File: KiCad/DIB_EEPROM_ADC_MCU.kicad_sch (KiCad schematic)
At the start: 63 parts, among them IC1 ADS131A04IPBSR, IC2 ISO6762FDWR, IC3 ISO6762FDWR, IC4 STM32H503CBT6, IC5 M24C32-DFDW6TP, X1 Edge connector, X2 N.C., Y1 ECS-163.84-10-33-JGN-TR, Y2 ABM8-25.000MHZ-D2X-T

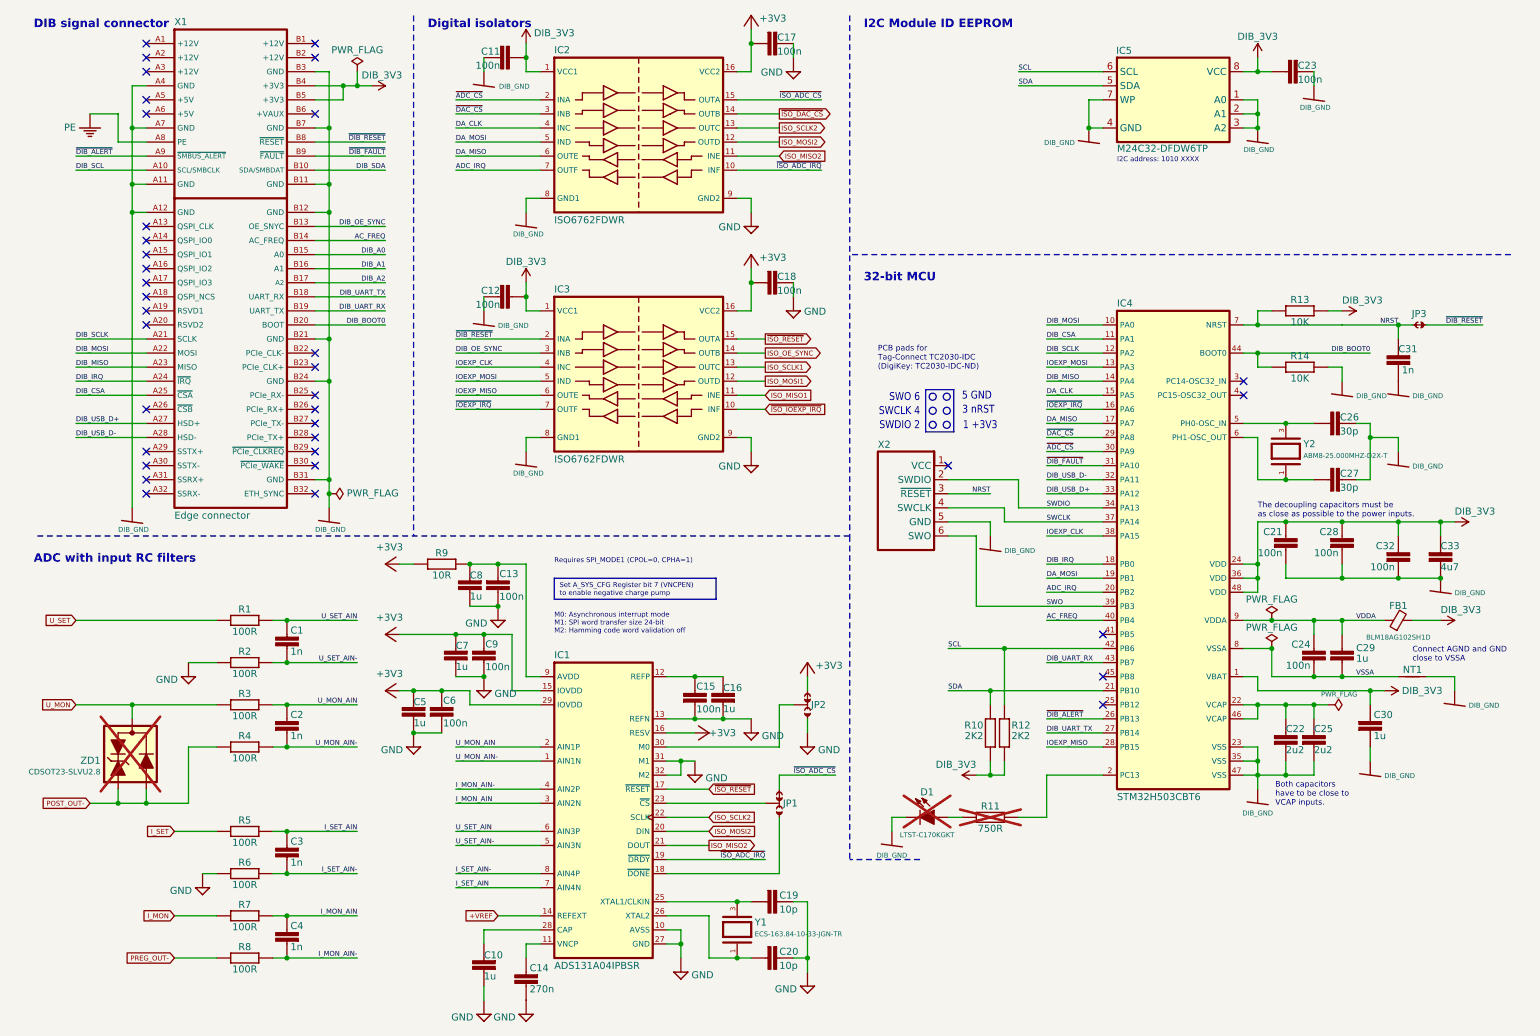
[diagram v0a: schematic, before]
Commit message: Additional 2 ch isolator added for OEP and temp sensor CS
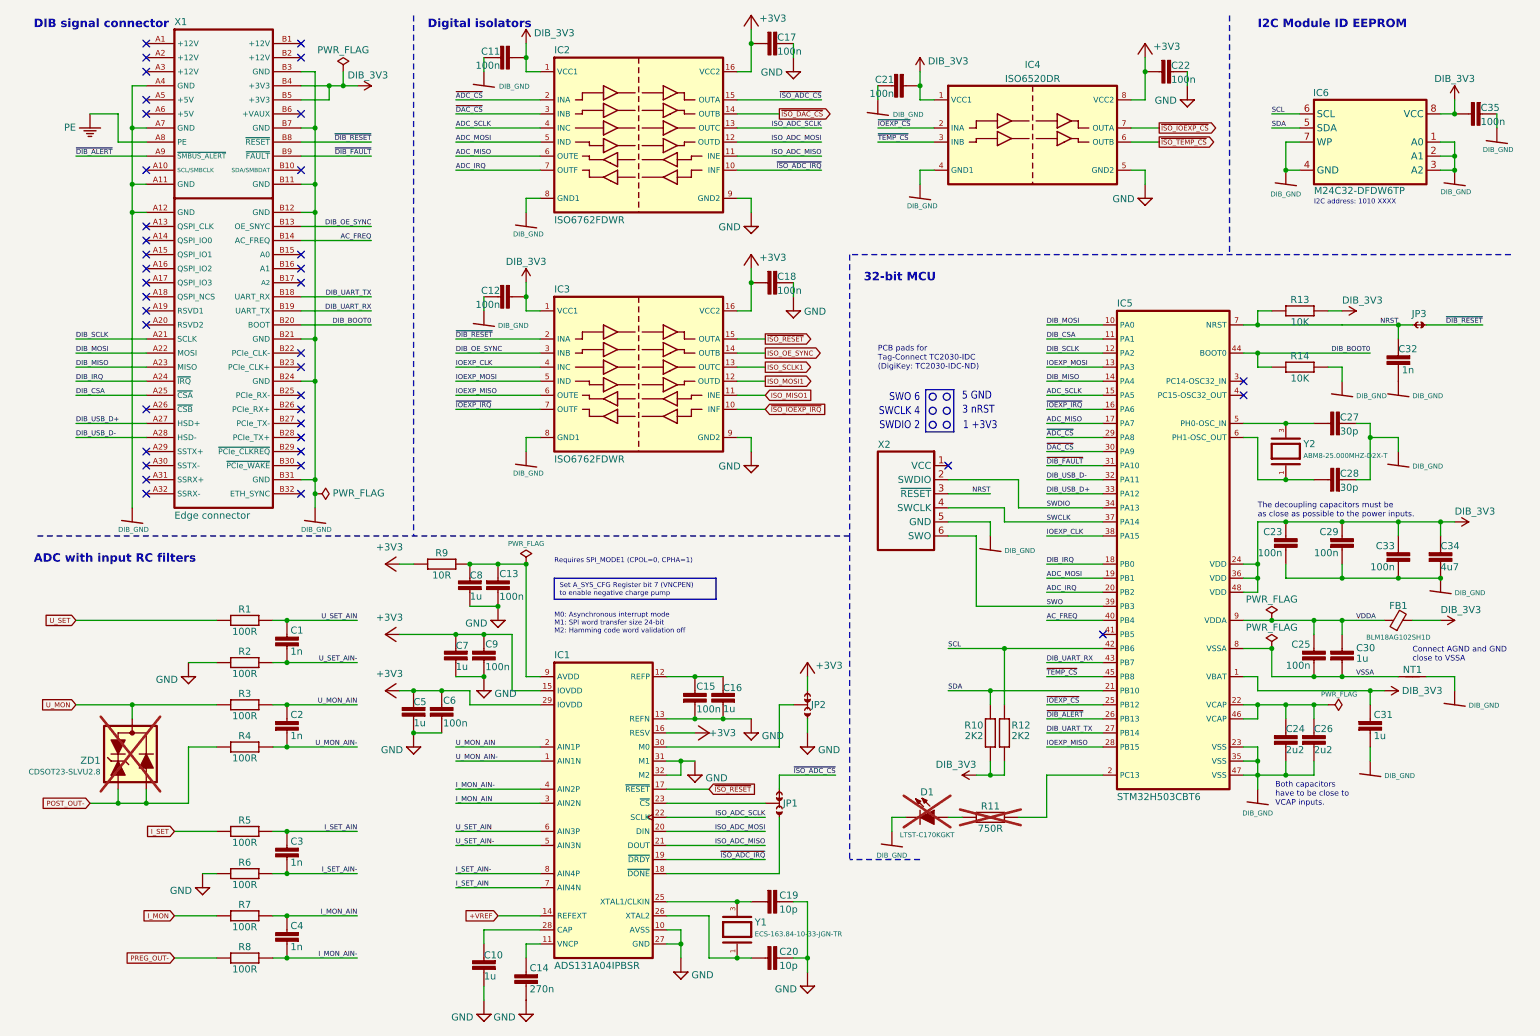
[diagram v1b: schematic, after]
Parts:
- added C21, C22: 100n, PCM_EEZ_passives:C_0603_1608Metric, symbol PCM_EEZ_passives:C-EU
- added IC4: ISO6520DR, PCM_EEZ_SMD:SOIC127P600X173-8N, symbol PCM_EEZ_TI:ISO6520DR
- X1: now left out of the parts list
- renumbered C21 to C23, C22 to C24, C24 to C25, C25 to C26, C26 to C27, C27 to C28, C28 to C29, C29 to C30, C30 to C31, C31 to C32, C32 to C33, C33 to C34, C23 to C35, IC4 to IC5, IC5 to IC6
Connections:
- net +3V3: now also C22.2, IC4.8 (VCC2)
- net DIB_3V3: now also C21.2, IC4.1 (VCC1)
- net DIB_GND: now also C21.1, IC4.4 (GND1)
- net GND: now also C22.1, IC4.5 (GND2)
- net ~{ADC_CS}: now also IC5.29 (PA8); no longer IC5.30 (PA9)
- net ~{DAC_CS}: now also IC5.30 (PA9); no longer IC5.29 (PA8)
- net ~{IOEXP_CS}: now reaches IC5.25 (PB12)
- net ~{IOEXP_CS}: now also IC4.2 (INA)
- net ~{TEMP_CS}: now reaches IC5.45 (PB8)
- net ~{TEMP_CS}: now also IC4.3 (INB)
- net DA_CLK renamed ADC_SCLK
- net DA_MISO renamed ADC_MISO
- net DA_MOSI renamed ADC_MOSI
- net DIB_A0: no longer names the net of X1.B15 (A0)
- net DIB_A1: no longer names the net of X1.B16 (A1)
- net DIB_A2: no longer names the net of X1.B17 (A2)
- net DIB_SCL: no longer names the net of X1.A10 (SCL/SMBCLK)
- net DIB_SDA: no longer names the net of X1.B10 (SDA/SMBDAT)
- net ISO_MISO2 renamed ISO_ADC_MISO
- net ISO_MOSI2 renamed ISO_ADC_MOSI
- net ISO_SCLK2 renamed ISO_ADC_SCLK
- new net ~{ISO_IOEXP_CS}: IC4.7 (OUTA)
- new net ~{ISO_TEMP_CS}: IC4.6 (OUTB)
- no-connect marks 36 -> 39
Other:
- moved on the sheet: C35, IC6, X1

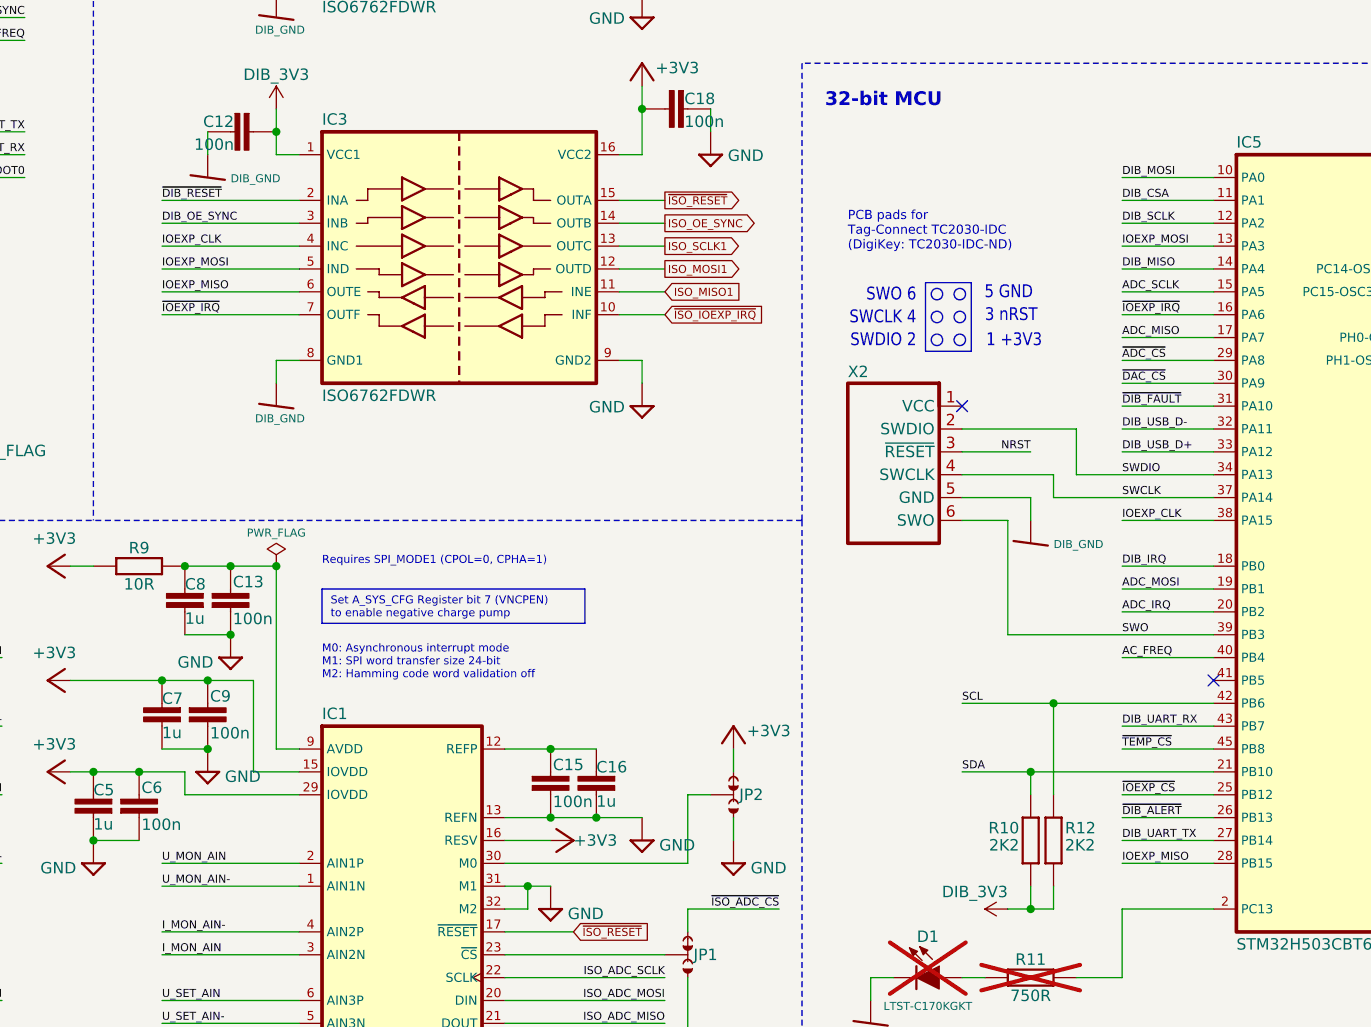
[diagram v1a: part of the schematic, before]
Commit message: DIB_MISO and DIB_MOSI swapped
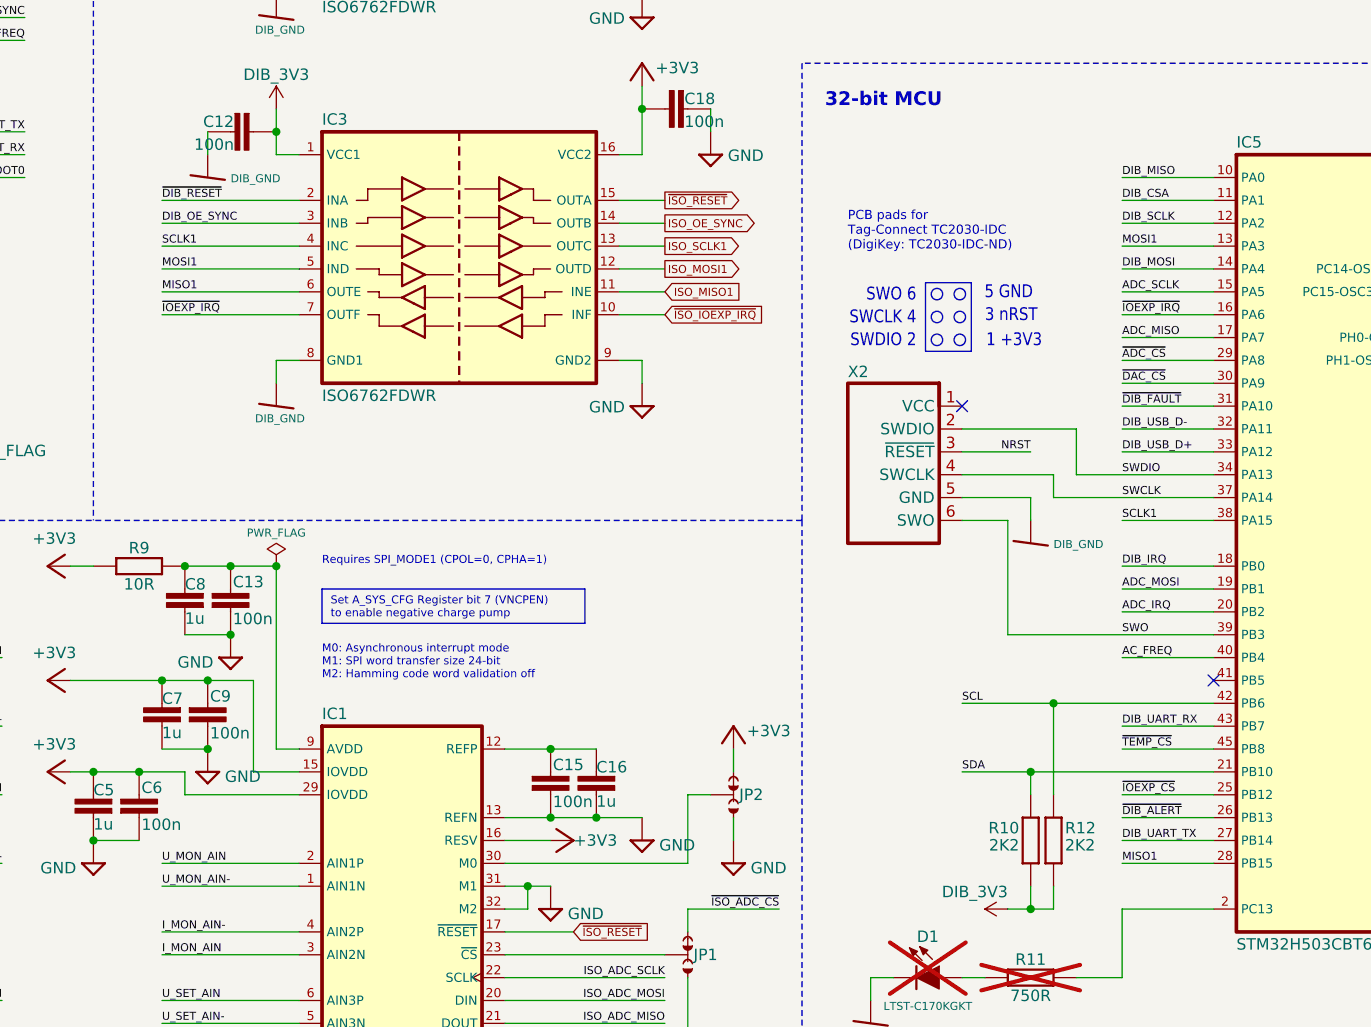
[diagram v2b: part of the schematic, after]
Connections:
- net DIB_MISO: now also IC5.10 (PA0); no longer IC5.14 (PA4)
- net DIB_MOSI: now also IC5.14 (PA4); no longer IC5.10 (PA0)
- net IOEXP_CLK renamed SCLK1
- net IOEXP_MISO renamed MISO1
- net IOEXP_MOSI renamed MOSI1
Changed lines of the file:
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@@
 	(title_block
 		(title "${project_name}")
-		(date "2025-12-08")
+		(date "2025-12-17")
 		(rev "${project_version}")
 		(company "${project_creator}")
@@
 	(wire
 		(pts
+			(xy 198.12 71.12) (xy 208.28 71.12)
+		)
+		(stroke
+			(width 0)
+			(type default)
+		)
+	)
+	(wire
+		(pts
 			(xy 91.44 78.74) (xy 106.68 78.74)
 		)
@@
 	(wire
 		(pts
+			(xy 198.12 81.28) (xy 208.28 81.28)
+		)
+		(stroke
+			(width 0)
+			(type default)
+		)
+	)
+	(wire
+		(pts
 			(xy 101.6 137.16) (xy 106.68 137.16)
 		)
@@
 	(wire
 		(pts
-			(xy 198.12 71.12) (xy 208.28 71.12)
-		)
-		(stroke
-			(width 0)
-			(type default)
-		)
-	)
-	(wire
-		(pts
 			(xy 180.34 106.68) (xy 187.96 106.68)
 		)
@@
 	(wire
 		(pts
-			(xy 198.12 81.28) (xy 208.28 81.28)
-		)
-		(stroke
-			(width 0)
-			(type default)
-		)
-	)
-	(wire
-		(pts
 			(xy 22.86 83.82) (xy 35.56 83.82)
 		)
@@
 		)
 	)
-	(label "IOEXP_MOSI"
+	(label "MOSI1"
 		(at 198.12 78.74 0)
 		(effects
@@
 		)
 	)
-	(label "IOEXP_MOSI"
+	(label "MOSI1"
 		(at 91.44 81.28 0)
 		(effects
@@
 		)
 	)
-	(label "IOEXP_CLK"
+	(label "SCLK1"
 		(at 198.12 109.22 0)
 		(effects
@@
 		)
 	)
-	(label "IOEXP_CLK"
+	(label "SCLK1"
 		(at 91.44 78.74 0)
 		(effects
@@
 		)
 	)
-	(label "IOEXP_MISO"
+	(label "MISO1"
 		(at 91.44 83.82 0)
 		(effects
@@
 		)
 	)
-	(label "IOEXP_MISO"
+	(label "MISO1"
 		(at 198.12 147.32 0)
 		(effects
@@
 	)
 	(label "DIB_MOSI"
-		(at 198.12 71.12 0)
+		(at 198.12 81.28 0)
 		(effects
 			(font
@@
 	)
 	(label "DIB_MISO"
-		(at 198.12 81.28 0)
+		(at 198.12 71.12 0)
 		(effects
 			(font
@@
 		(on_board yes)
 		(dnp no)
-		(property "Reference" "#FLG03"
+		(property "Reference" "#FLG04"
 			(at 238.76 122.555 0)
 			(effects
@@
 			(project "EEZ DIB2 DCP426"
 				(path "/65943c0e-8943-4d2a-93dc-fb4938f73312/becc625c-e1bd-41b9-8b5b-ca8fa1d0ce1c"
-					(reference "#FLG03")
+					(reference "#FLG04")
 					(unit 1)
 				)
@@
 		(on_board yes)
 		(dnp no)
-		(property "Reference" "#FLG016"
+		(property "Reference" "#FLG03"
 			(at 104.14 112.395 0)
 			(effects
@@
 			(project "EEZ DIB DCP405plus"
 				(path "/65943c0e-8943-4d2a-93dc-fb4938f73312/becc625c-e1bd-41b9-8b5b-ca8fa1d0ce1c"
-					(reference "#FLG016")
+					(reference "#FLG03")
 					(unit 1)
 				)
@@
 		(on_board yes)
 		(dnp no)
-		(property "Reference" "#FLG04"
+		(property "Reference" "#FLG05"
 			(at 238.76 127.635 0)
 			(effects
@@
 			(project "EEZ DIB2 DCP426"
 				(path "/65943c0e-8943-4d2a-93dc-fb4938f73312/becc625c-e1bd-41b9-8b5b-ca8fa1d0ce1c"
-					(reference "#FLG04")
+					(reference "#FLG05")
 					(unit 1)
 				)
@@
 		(on_board yes)
 		(dnp no)
-		(property "Reference" "#FLG05"
+		(property "Reference" "#FLG06"
 			(at 250.825 139.7 0)
 			(effects
@@
 			(project "EEZ DIB2 DCP426"
 				(path "/65943c0e-8943-4d2a-93dc-fb4938f73312/becc625c-e1bd-41b9-8b5b-ca8fa1d0ce1c"
-					(reference "#FLG05")
+					(reference "#FLG06")
 					(unit 1)
 				)
